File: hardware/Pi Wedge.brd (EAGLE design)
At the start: 40.6 x 40.6 mm, 9 parts

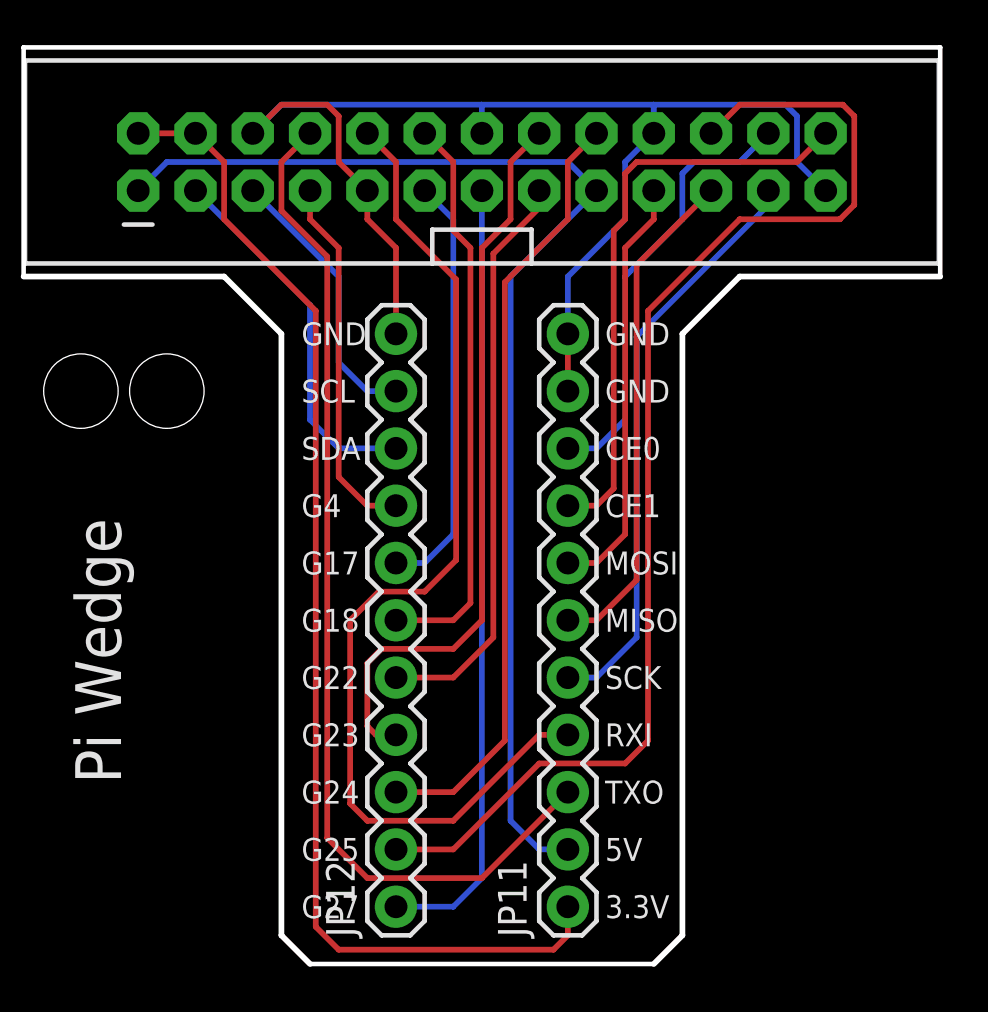
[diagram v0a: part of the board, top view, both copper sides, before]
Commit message: Correcting footprint
The front and back rows needed to be swapped to work with the SparkFun
23 pin ribbon.
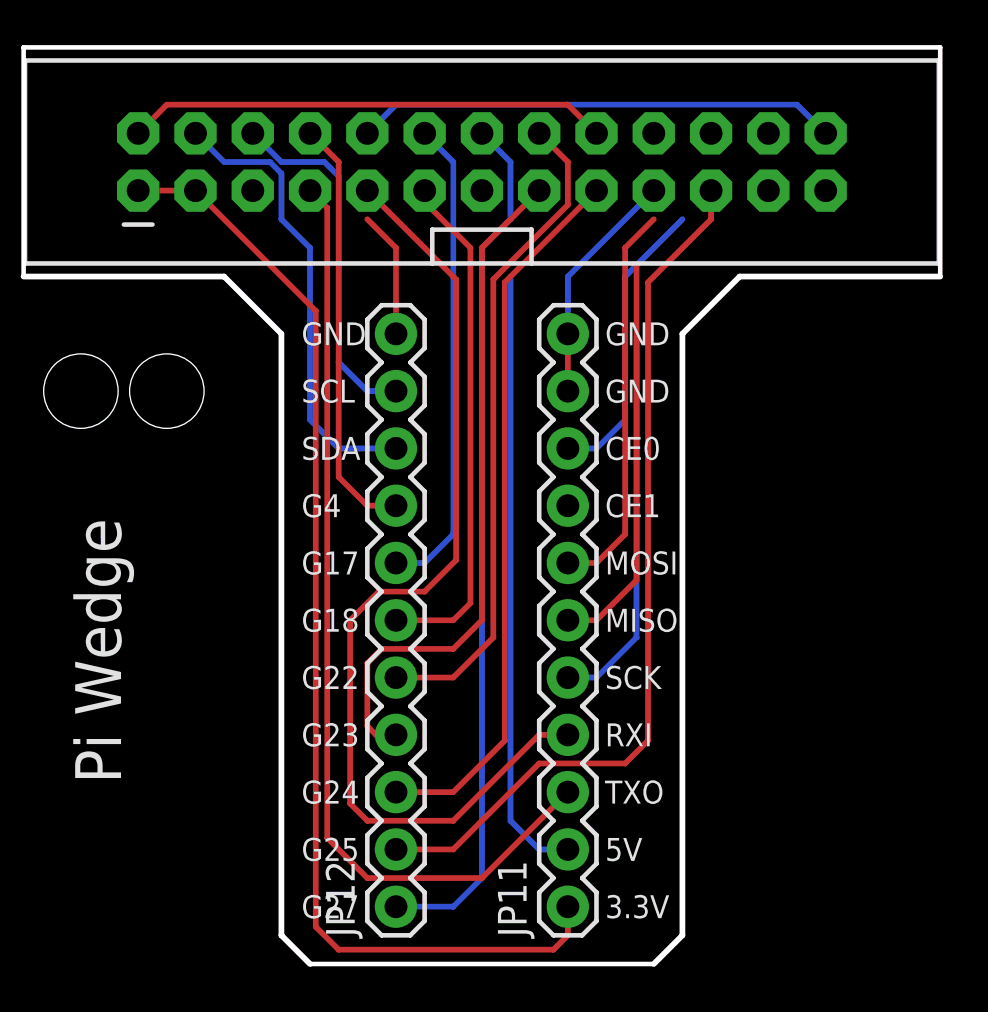
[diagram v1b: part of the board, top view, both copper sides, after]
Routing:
- net CE1: track 26.2 -> 0.00 mm
- net GND: track 59.5 -> 37.4 mm
- net GP25: track 54.3 -> 38.7 mm
- net SCLK: track 26.0 -> 17.1 mm
- net CE2: track 19.6 -> 13.0 mm
- net 5V: track 54.0 -> 48.6 mm
- net MISO: track 22.4 -> 17.8 mm
- net SDA: track 16.6 -> 20.3 mm
- net SCL: track 12.3 -> 15.9 mm
- net TXO: track 45.6 -> 42.0 mm
- net GP27: track 34.8 -> 38.4 mm
- net GP22: track 25.7 -> 29.3 mm
- net GP4: track 16.3 -> 18.8 mm
- net GP23: track 32.7 -> 30.2 mm
- net GP24: track 34.4 -> 31.8 mm
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
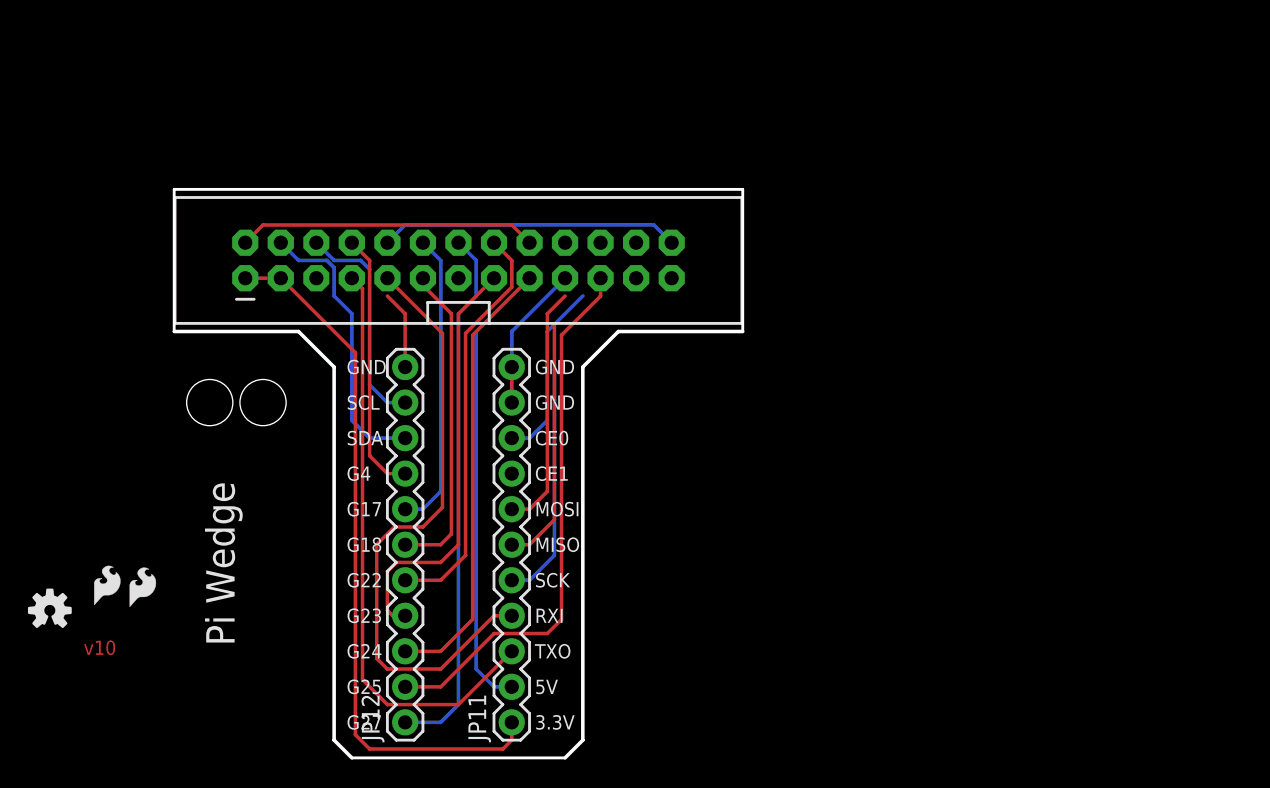
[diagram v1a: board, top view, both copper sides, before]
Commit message: Adjusting everything.
Reoriented connectors, added 6-pin FTDI header and extra access to power
and ground.
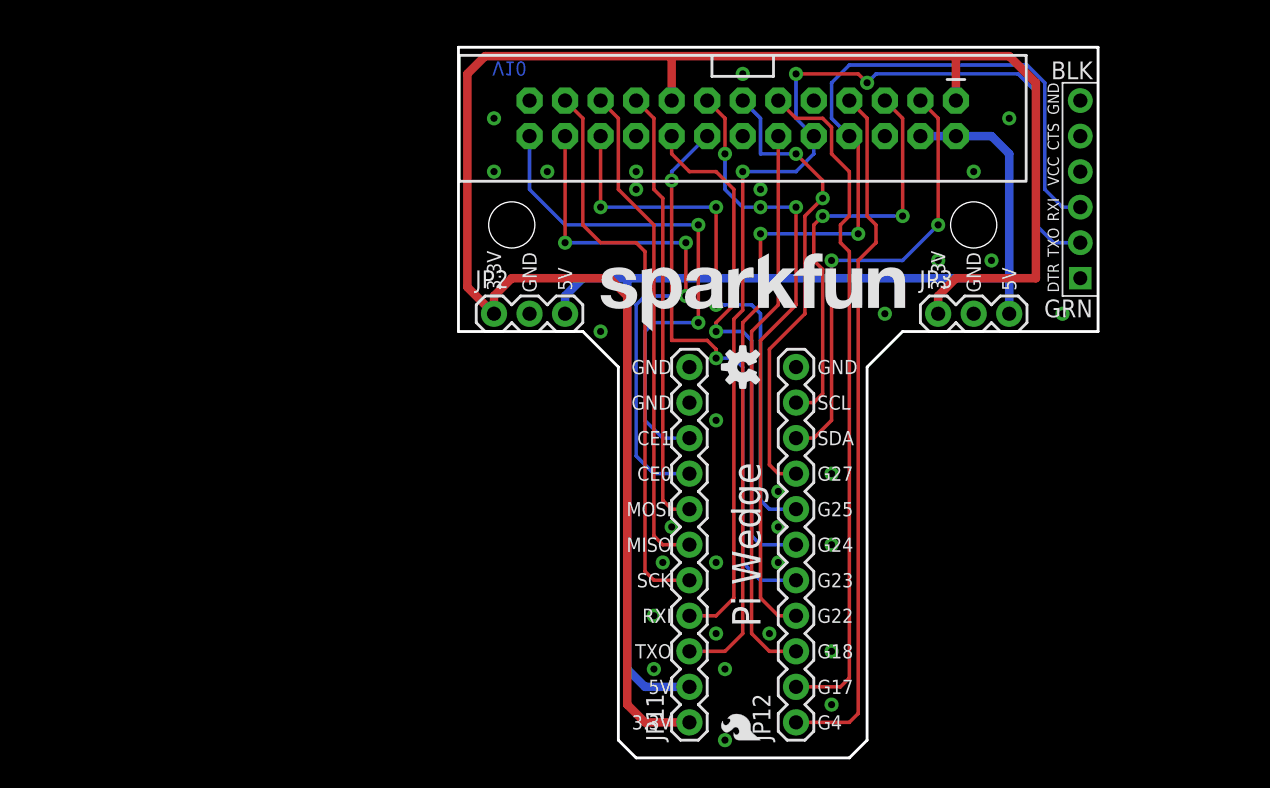
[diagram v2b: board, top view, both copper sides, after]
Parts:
- removed U$2: CREATIVE_COMMONS, SparkFun:CREATIVE_COMMONS
- added FRAME2: FRAME-LETTER, SparkFun-Aesthetics:CREATIVE_COMMONS
- added JP4: FTDI_DEVICE, SparkFun-Connectors:FTDI_DEVICE_SIDE
- added LOGO1: SFE_LOGO_NAME.2_INCH, SparkFun-Aesthetics:SFE_LOGO_NAME_.2
- added STANDOFF1, STANDOFF2: STAND-OFF, SparkFun-Electromechanical:STAND-OFF
- JP2, JP3: value STAND-OFF -> PWR; device SparkFun:STAND-OFF -> SparkFun-Connectors:1X03
- JP8: device Testing:2X13-SHROUDED -> SparkFun-Boards:2X13-SHROUDED
- moved U$1 52.5 mm to (20.3, 27.9), turned to 90 degrees
- moved JP3 52.5 mm to (34.3, 31.8), turned to 0 degrees
- moved JP1 48.6 mm to (21.6, 1.27), turned to 90 degrees
- moved JP5 45.5 mm to (21.0, 1.27), flipped to the bottom
- moved JP12 27.9 mm to (24.1, 2.54)
- moved JP8 22.7 mm to (20.3, 45.7), turned to 270 degrees
- moved JP2 17.7 mm to (2.54, 31.8), turned to 0 degrees
- moved JP11 12.7 mm to (16.5, 2.54)
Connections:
- removed net CE2: JP11.9, JP8.24
- removed net GP17: JP12.7, JP8.11
- removed net GP18: JP12.6, JP8.12
- removed net GP22: JP12.5, JP8.15
- removed net GP23: JP12.4, JP8.16
- removed net GP24: JP12.3, JP8.18
- removed net GP25: JP12.2, JP8.22
- removed net GP27: JP12.1, JP8.13
- removed net GP4: JP12.8, JP8.7
- new net CE0: JP11.8, JP8.24
- new net GPIO17: JP12.2, JP8.11
- new net GPIO18: JP12.3, JP8.12
- new net GPIO22: JP12.4, JP8.15
- new net GPIO23: JP12.5, JP8.16
- new net GPIO24: JP12.6, JP8.18
- new net GPIO25: JP12.7, JP8.22
- new net GPIO27: JP12.8, JP8.13
- new net GPIO4: JP12.1, JP8.7
- net 3.3V: now also JP2.1, JP3.1, JP8.1, JP8.17; no longer JP8.2, JP8.4
- net 5V: now also JP2.3, JP3.3, JP8.2, JP8.4; no longer JP8.1, JP8.17
- net CE1: now also JP11.9; no longer JP11.8
- net GND: now also JP2.2, JP3.2, JP4.P$6
- net RXI: now also JP4.P$2
- net TXO: now also JP4.P$3
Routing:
- net 3.3V: track 50.5 -> 135.0 mm
- net GPIO4: track 0.00 -> 49.8 mm
- net GPIO17: track 0.00 -> 49.1 mm
- net GPIO22: track 0.00 -> 44.5 mm, vias 0 -> 3
- net GPIO23: track 0.00 -> 40.2 mm, vias 0 -> 2
- net GPIO18: track 0.00 -> 40.1 mm
- net GPIO25: track 0.00 -> 39.9 mm, vias 0 -> 3
- net CE0: track 0.00 -> 39.0 mm, vias 0 -> 3
- net GP25: track 38.7 -> 0.00 mm
- net GP27: track 38.4 -> 0.00 mm
- net CE1: track 0.00 -> 38.0 mm, vias 0 -> 2
- net GPIO24: track 0.00 -> 37.7 mm, vias 0 -> 1
- net GND: track 37.4 -> 0.00 mm, vias 0 -> 31
- net TXO: track 42.0 -> 79.0 mm, vias 0 -> 2
- net 5V: track 48.6 -> 84.8 mm
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- added copper zone on layer 1, net GND
- added copper zone on layer 16, net GND
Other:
- board size 40.6 x 40.6 mm -> 45.7 x 50.8 mm
- board text added: "Byron Jacquot"
- board text added: "V10"
- board text removed: "v10"

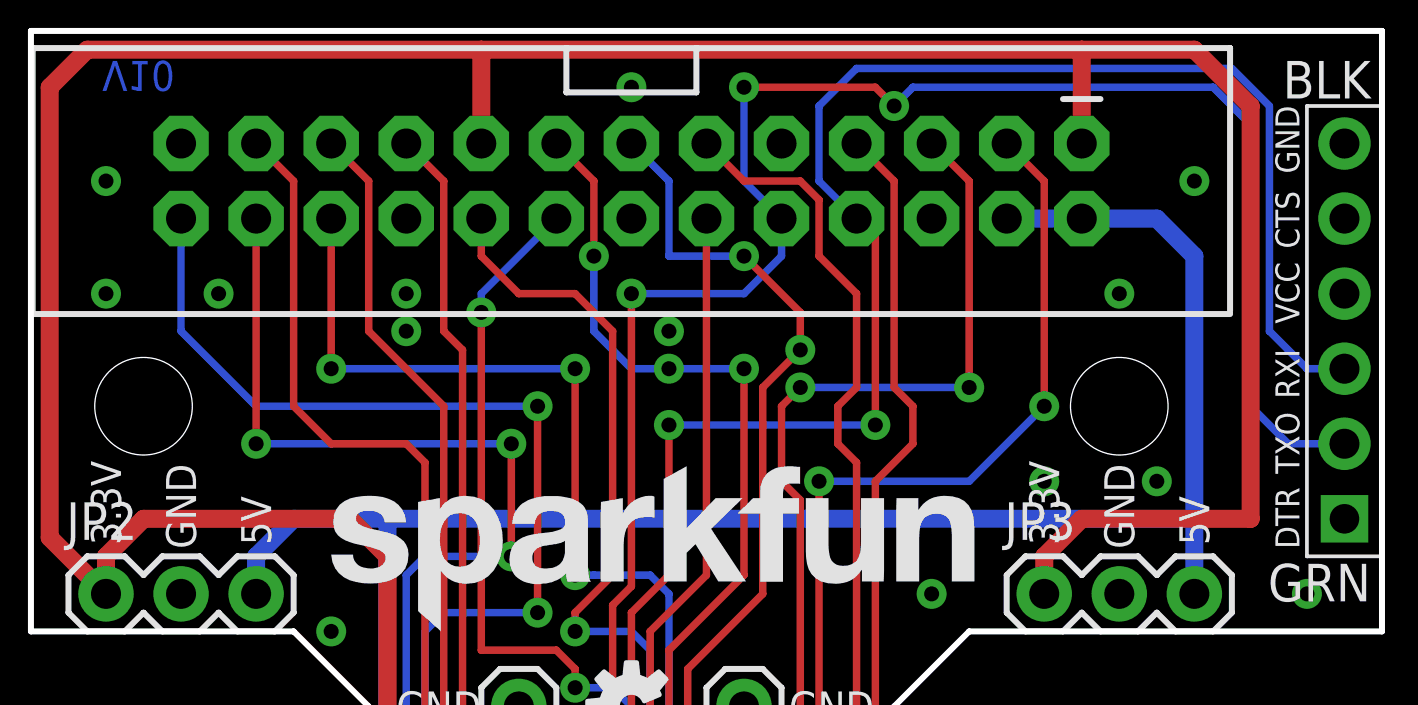
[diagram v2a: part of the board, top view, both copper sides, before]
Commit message: Fixing keepout violations around mtg holes
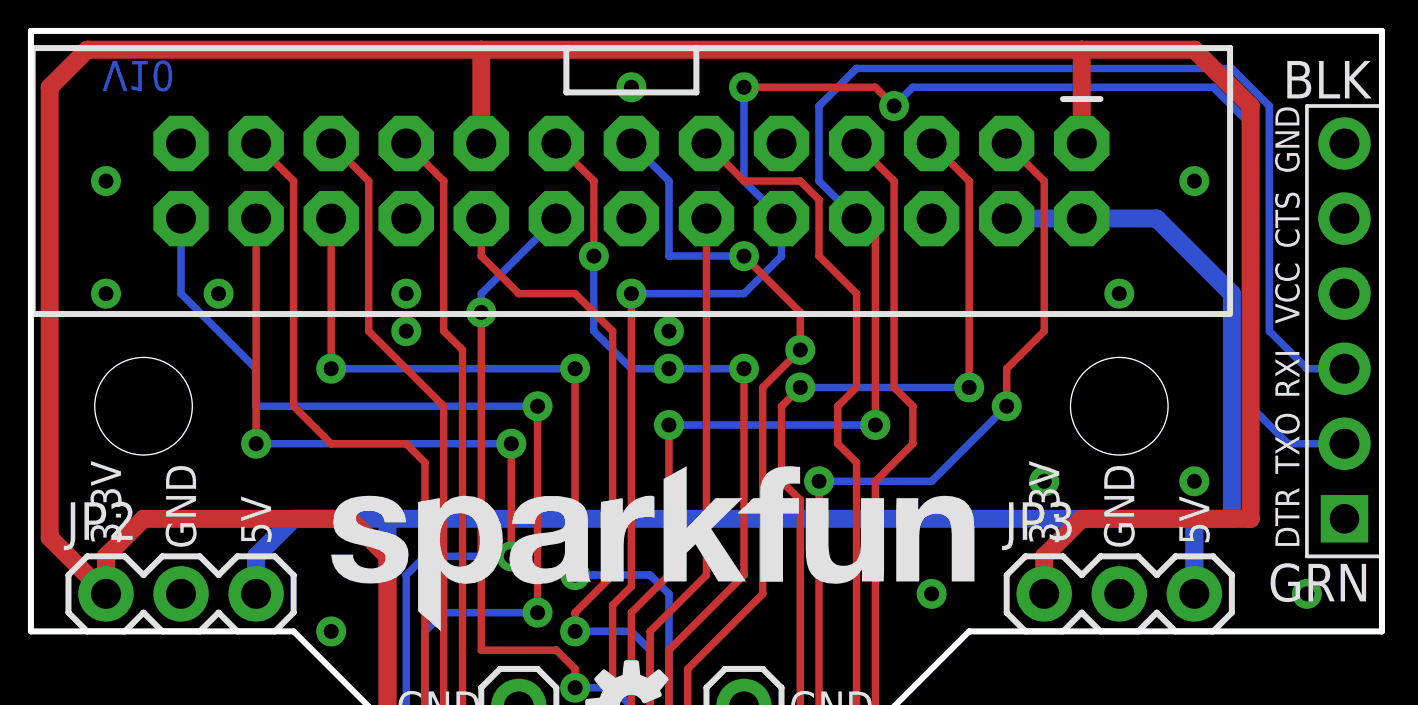
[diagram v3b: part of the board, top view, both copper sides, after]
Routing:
- net 5V: track 84.8 -> 86.6 mm
- net SDA: track 32.6 -> 31.8 mm
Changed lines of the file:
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@@
 <layer number="37" name="tTest" color="7" fill="1" visible="no" active="yes"/>
 <layer number="38" name="bTest" color="7" fill="1" visible="no" active="yes"/>
-<layer number="39" name="tKeepout" color="4" fill="11" visible="no" active="yes"/>
+<layer number="39" name="tKeepout" color="4" fill="11" visible="yes" active="yes"/>
 <layer number="40" name="bKeepout" color="1" fill="11" visible="no" active="yes"/>
 <layer number="41" name="tRestrict" color="4" fill="10" visible="no" active="yes"/>
@@
 <layer number="43" name="vRestrict" color="2" fill="10" visible="no" active="yes"/>
 <layer number="44" name="Drills" color="7" fill="1" visible="no" active="yes"/>
-<layer number="45" name="Holes" color="7" fill="1" visible="no" active="yes"/>
+<layer number="45" name="Holes" color="7" fill="1" visible="yes" active="yes"/>
 <layer number="46" name="Milling" color="3" fill="1" visible="no" active="yes"/>
 <layer number="47" name="Measures" color="7" fill="1" visible="no" active="yes"/>
 <layer number="48" name="Document" color="7" fill="1" visible="no" active="yes"/>
-<layer number="49" name="Reference" color="7" fill="1" visible="no" active="yes"/>
+<layer number="49" name="Reference" color="7" fill="1" visible="yes" active="yes"/>
 <layer number="50" name="dxf" color="7" fill="1" visible="no" active="yes"/>
 <layer number="51" name="tDocu" color="6" fill="1" visible="yes" active="yes"/>
@@
 <text x="15.24" y="2.54" size="1.016" layer="21" ratio="19" rot="SR0" align="center-right">3.3V</text>
 <dimension x1="11.43" y1="1.27" x2="29.21" y2="1.27" x3="20.32" y3="-5.08" textsize="1.778" textratio="15" layer="47" unit="inch"/>
-<text x="5.588" y="33.274" size="1.016" layer="21" ratio="19" rot="SR90">GND</text>
-<text x="37.338" y="33.274" size="1.016" layer="21" ratio="19" rot="SR90">GND</text>
+<text x="5.588" y="33.274" size="1.016" layer="21" font="vector" ratio="19" rot="SR90">GND</text>
+<text x="37.338" y="33.274" size="1.016" layer="21" font="vector" ratio="19" rot="SR90">GND</text>
 <text x="34.798" y="33.401" size="1.016" layer="21" ratio="19" rot="SR90">3.3V</text>
 <text x="3.048" y="33.401" size="1.016" layer="21" ratio="19" rot="SR90">3.3V</text>
@@
 <wire x1="26.67" y1="24.13" x2="26.67" y2="35.56" width="0.254" layer="1"/>
 <via x="26.67" y="35.56" extent="1-16" drill="0.508"/>
-<wire x1="26.67" y1="35.56" x2="31.75" y2="35.56" width="0.254" layer="16"/>
-<wire x1="31.75" y1="35.56" x2="34.29" y2="38.1" width="0.254" layer="16"/>
-<via x="34.29" y="38.1" extent="1-16" drill="0.508"/>
-<wire x1="34.29" y1="38.1" x2="34.29" y2="45.72" width="0.254" layer="1"/>
+<wire x1="26.67" y1="35.56" x2="30.48" y2="35.56" width="0.254" layer="16"/>
+<wire x1="30.48" y1="35.56" x2="33.02" y2="38.1" width="0.254" layer="16"/>
+<via x="33.02" y="38.1" extent="1-16" drill="0.508"/>
+<wire x1="33.02" y1="38.1" x2="33.02" y2="39.37" width="0.254" layer="1"/>
+<wire x1="33.02" y1="39.37" x2="34.29" y2="40.64" width="0.254" layer="1"/>
+<wire x1="34.29" y1="40.64" x2="34.29" y2="45.72" width="0.254" layer="1"/>
 <wire x1="34.29" y1="45.72" x2="33.02" y2="46.99" width="0.254" layer="1"/>
 </signal>
@@
 <via x="18.415" y="24.13" extent="1-16" drill="0.508"/>
 <via x="34.29" y="35.56" extent="1-16" drill="0.508"/>
-<via x="38.1" y="35.56" extent="1-16" drill="0.508"/>
+<via x="39.37" y="35.56" extent="1-16" drill="0.508"/>
 <via x="2.54" y="41.91" extent="1-16" drill="0.508"/>
 </signal>
@@
 <contactref element="JP8" pad="4"/>
 <contactref element="JP8" pad="2"/>
-<wire x1="39.37" y1="43.18" x2="38.1" y2="44.45" width="0.6096" layer="16"/>
+<wire x1="40.64" y1="41.91" x2="38.1" y2="44.45" width="0.6096" layer="16"/>
 <wire x1="38.1" y1="44.45" x2="35.56" y2="44.45" width="0.6096" layer="16"/>
 <wire x1="33.02" y1="44.45" x2="35.56" y2="44.45" width="0.6096" layer="16"/>
 <contactref element="JP3" pad="3"/>
 <contactref element="JP2" pad="3"/>
-<wire x1="39.37" y1="34.29" x2="39.37" y2="43.18" width="0.6096" layer="16"/>
+<wire x1="40.64" y1="34.29" x2="40.64" y2="41.91" width="0.6096" layer="16"/>
 <wire x1="39.37" y1="31.75" x2="39.37" y2="34.29" width="0.6096" layer="16"/>
+<wire x1="39.37" y1="34.29" x2="40.64" y2="34.29" width="0.6096" layer="16"/>
 <wire x1="7.62" y1="31.75" x2="7.62" y2="33.02" width="0.6096" layer="16"/>
 <wire x1="7.62" y1="33.02" x2="8.89" y2="34.29" width="0.6096" layer="16"/>
@@
 <via x="17.145" y="38.1" extent="1-16" drill="0.508"/>
 <wire x1="17.145" y1="38.1" x2="7.62" y2="38.1" width="0.254" layer="16"/>
-<wire x1="7.62" y1="38.1" x2="5.08" y2="40.64" width="0.254" layer="16"/>
-<wire x1="5.08" y1="40.64" x2="5.08" y2="44.45" width="0.254" layer="16"/>
+<wire x1="7.62" y1="38.1" x2="7.62" y2="39.37" width="0.254" layer="16"/>
+<wire x1="7.62" y1="39.37" x2="5.08" y2="41.91" width="0.254" layer="16"/>
+<wire x1="5.08" y1="41.91" x2="5.08" y2="44.45" width="0.254" layer="16"/>
 </signal>
 <signal name="GPIO4">
